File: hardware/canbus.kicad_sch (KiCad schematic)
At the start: 21 parts, among them U5 MCP2515-xSO, U6 MCP2551-I/SN, Y2 16MHz

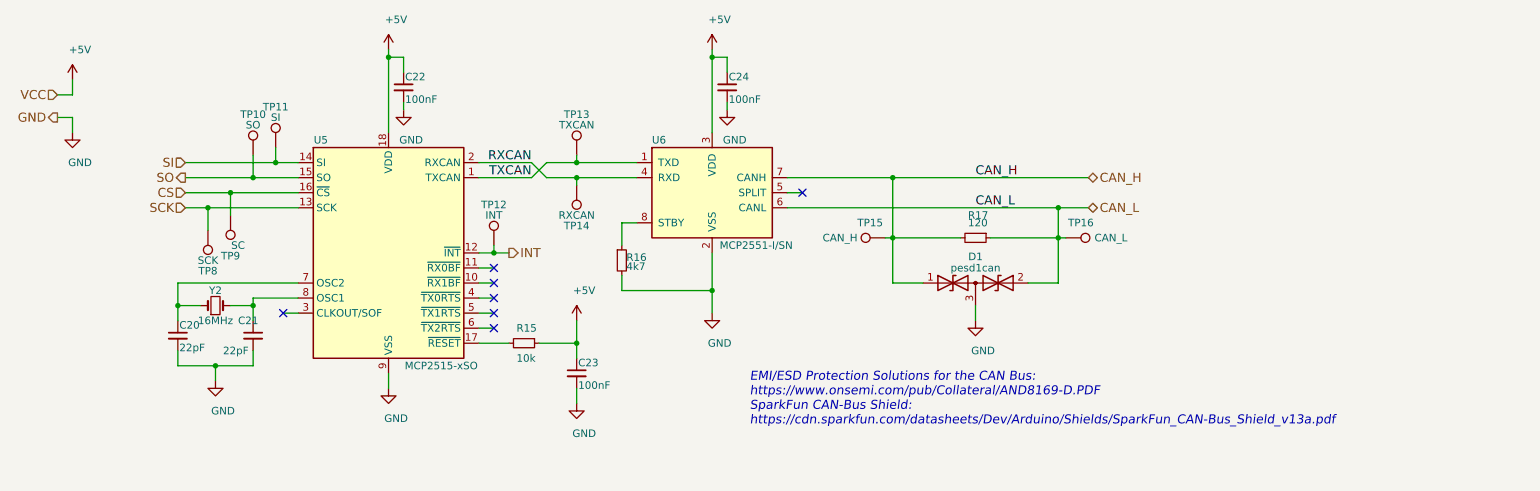
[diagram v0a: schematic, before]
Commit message: Troca do atmega328p -> STM32F103C8T Já que tem CAN integrado e ADC 12 bits (ao invés de 10)
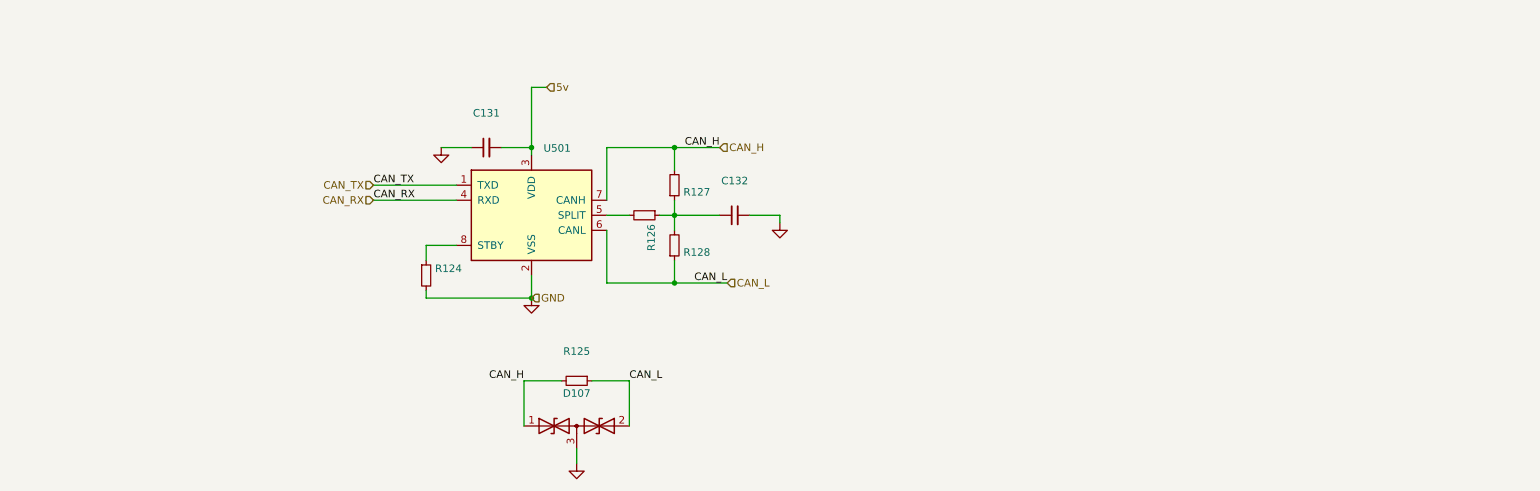
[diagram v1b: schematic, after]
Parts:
- removed C20, C21: 22pF, Capacitor_SMD:C_0805_2012Metric_Pad1.18x1.45mm_HandSolder, symbol Device:C_Small
- removed C22, C23, C24: 100nF, Capacitor_SMD:C_0805_2012Metric_Pad1.18x1.45mm_HandSolder, symbol Device:C_Small
- removed D1: pesd1can, Package_TO_SOT_SMD:SOT-23_Handsoldering, symbol Device:D_TVS_Dual_AAC
- removed R15: 10k, Resistor_SMD:R_0805_2012Metric_Pad1.20x1.40mm_HandSolder, symbol Device:R_Small
- removed R16: 4k7, Resistor_SMD:R_0805_2012Metric_Pad1.20x1.40mm_HandSolder, symbol Device:R_Small
- removed R17: 120, Resistor_SMD:R_0805_2012Metric_Pad1.20x1.40mm_HandSolder, symbol Device:R_Small
- removed TP10: SO, TestPoint:TestPoint_Pad_2.0x2.0mm, symbol Connector:TestPoint
- removed TP11: SI, TestPoint:TestPoint_Pad_2.0x2.0mm, symbol Connector:TestPoint
- removed TP12: INT, TestPoint:TestPoint_Pad_2.0x2.0mm, symbol Connector:TestPoint
- removed TP13: TXCAN, TestPoint:TestPoint_Pad_2.0x2.0mm, symbol Connector:TestPoint
- removed TP14: RXCAN, TestPoint:TestPoint_Pad_2.0x2.0mm, symbol Connector:TestPoint
- removed TP15: CAN_H, TestPoint:TestPoint_Pad_2.0x2.0mm, symbol Connector:TestPoint
- removed TP16: CAN_L, TestPoint:TestPoint_Pad_2.0x2.0mm, symbol Connector:TestPoint
- removed TP8: SCK, TestPoint:TestPoint_Pad_2.0x2.0mm, symbol Connector:TestPoint
- removed TP9: SC, TestPoint:TestPoint_Pad_2.0x2.0mm, symbol Connector:TestPoint
- removed U5: MCP2515-xSO, Package_SO:SOIC-18W_7.5x11.6mm_P1.27mm, symbol Interface_CAN_LIN:MCP2515-xSO
- removed U6: MCP2551-I/SN, Package_SO:SOIC-8_3.9x4.9mm_P1.27mm, symbol Interface_CAN_LIN:MCP2561-E-SN
- removed Y2: 16MHz, Crystal:Crystal_HC49-U_Vertical, symbol Device:Crystal_Small
- added C131, C132: (no value), symbol Device:C_Small
- added D107: ~, symbol Controle-rescue:D_TVS_x2_AAC-Device
- added R124, R125, R126, R127, R128: (no value), symbol Device:R_Small
- added U501: (no value), symbol Interface_CAN_LIN:MCP2561-E-SN
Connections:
- net CAN_H: now also D107.1 (A1), R125.2, R127.2, U501.7 (CANH)
- net CAN_L: now also D107.2 (A2), R125.1, R128.1, U501.6 (CANL)
- net GND: now also C131.1, C132.2, D107.3 (common), R124.2, U501.2 (VSS)
- new net: R124.1, U501.8 (STBY)
- new net: C132.1, R126.1, R127.1, R128.2
- new net: R126.2, U501.5 (SPLIT)
- new net 5v: C131.2, U501.3 (VDD)
- new net CAN_RX: U501.4 (RXD)
- new net CAN_TX: U501.1 (TXD)
- no-connect marks 7 -> 0
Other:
- note removed: "EMI/ESD Protection Solutions for the CAN Bus: https://www.onsemi.com/pub/Collateral/AND8169-D.PDF SparkFun CAN-Bus Shield: https://cdn.sparkfun.com/datasheets/Dev/Arduino/Shields/SparkFun_CAN-Bus_Shield_v13a.pdf"

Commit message: Primeiro protótipo da PCB
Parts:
- added TP501, TP502, TP503, TP504: (no value), symbol Connector:TestPoint
- C131: value (none) -> 100n; footprint (none) -> Capacitor_SMD:C_0603_1608Metric_Pad1.08x0.95mm_HandSolder
- C132: value (none) -> 4.7n; footprint (none) -> Capacitor_SMD:C_0603_1608Metric_Pad1.08x0.95mm_HandSolder
- D107: value ~ -> (none)
- R124: value (none) -> 4k7; footprint (none) -> Resistor_SMD:R_0603_1608Metric_Pad0.98x0.95mm_HandSolder
- R125: value (none) -> NC; footprint (none) -> Resistor_SMD:R_0603_1608Metric_Pad0.98x0.95mm_HandSolder
- R126: value (none) -> 300; footprint (none) -> Resistor_SMD:R_0603_1608Metric_Pad0.98x0.95mm_HandSolder
- R127, R128: value (none) -> 520; footprint (none) -> Resistor_SMD:R_0603_1608Metric_Pad0.98x0.95mm_HandSolder
- U501: value (none) -> MCP2561-E-SN; footprint (none) -> Package_SO:SOIC-8_3.9x4.9mm_P1.27mm
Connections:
- net CAN_H: now also TP503.1
- net CAN_L: now also TP504.1
- net CAN_RX: now also TP502.1
- net CAN_TX: now also TP501.1
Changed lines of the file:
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@@
   (junction (at 157.48 87.63) (diameter 0) (color 0 0 0 0)
   )
+  (junction (at 110.49 82.55) (diameter 0) (color 0 0 0 0)
+  )
   (junction (at 133.35 101.6) (diameter 0) (color 0 0 0 0)
   )
   (junction (at 133.35 76.2) (diameter 0) (color 0 0 0 0)
   )
+  (junction (at 110.49 85.09) (diameter 0) (color 0 0 0 0)
+  )
   (wire (pts (xy 133.35 101.6) (xy 133.35 97.79))
     (stroke (width 0) (type default) (color 0 0 0 0))
@@
     (stroke (width 0) (type default) (color 0 0 0 0))
   )
+  (wire (pts (xy 110.49 82.55) (xy 106.68 82.55))
+    (stroke (width 0) (type default) (color 0 0 0 0))
+  )
   (wire (pts (xy 140.97 129.54) (xy 140.97 127))
     (stroke (width 0) (type default) (color 0 0 0 0))
@@
     (stroke (width 0) (type default) (color 0 0 0 0))
   )
-  (wire (pts (xy 120.65 82.55) (xy 106.68 82.55))
+  (wire (pts (xy 120.65 82.55) (xy 110.49 82.55))
     (stroke (width 0) (type default) (color 0 0 0 0))
   )
@@
     (stroke (width 0) (type default) (color 0 0 0 0))
   )
+  (wire (pts (xy 110.49 85.09) (xy 106.68 85.09))
+    (stroke (width 0) (type default) (color 0 0 0 0))
+  )
   (wire (pts (xy 133.35 66.04) (xy 135.89 66.04))
     (stroke (width 0) (type default) (color 0 0 0 0))
@@
     (stroke (width 0) (type default) (color 0 0 0 0))
   )
-  (wire (pts (xy 120.65 85.09) (xy 106.68 85.09))
+  (wire (pts (xy 120.65 85.09) (xy 110.49 85.09))
     (stroke (width 0) (type default) (color 0 0 0 0))
   )
@@
       (effects (font (size 1.27 1.27)) (justify left))
     )
-    (property "Value" "" (id 1) (at 117.0686 98.933 0)
-      (effects (font (size 1.27 1.27)) (justify left))
-    )
-    (property "Footprint" "" (id 2) (at 115.57 97.79 0)
+    (property "Value" "4k7" (id 1) (at 117.0686 98.933 0)
+      (effects (font (size 1.27 1.27)) (justify left))
+    )
+    (property "Footprint" "Resistor_SMD:R_0603_1608Metric_Pad0.98x0.95mm_HandSolder" (id 2) (at 115.57 97.79 0)
       (effects (font (size 1.27 1.27)) hide)
     )
@@
     (in_bom yes) (on_board yes)
     (property "Reference" "C131" (id 0) (at 125.73 70.3834 90))
-    (property "Value" "" (id 1) (at 125.73 72.6948 90))
-    (property "Footprint" "" (id 2) (at 125.73 76.2 0)
+    (property "Value" "100n" (id 1) (at 125.73 72.6948 90))
+    (property "Footprint" "Capacitor_SMD:C_0603_1608Metric_Pad1.08x0.95mm_HandSolder" (id 2) (at 125.73 76.2 0)
       (effects (font (size 1.27 1.27)) hide)
     )
@@
     (in_bom yes) (on_board yes)
     (property "Reference" "D107" (id 0) (at 140.97 117.6782 0))
-    (property "Value" "~" (id 1) (at 140.97 119.9896 0))
+    (property "Value" "" (id 1) (at 140.97 119.9896 0))
     (property "Footprint" "" (id 2) (at 140.97 123.19 0)
       (effects (font (size 1.27 1.27)) hide)
@@
     (in_bom yes) (on_board yes)
     (property "Reference" "R125" (id 0) (at 140.97 110.5916 90))
-    (property "Value" "" (id 1) (at 140.97 112.903 90))
-    (property "Footprint" "" (id 2) (at 140.97 115.57 0)
+    (property "Value" "NC" (id 1) (at 140.97 112.903 90))
+    (property "Footprint" "Resistor_SMD:R_0603_1608Metric_Pad0.98x0.95mm_HandSolder" (id 2) (at 140.97 115.57 0)
       (effects (font (size 1.27 1.27)) hide)
     )
@@
       (effects (font (size 1.27 1.27)) (justify left))
     )
-    (property "Value" "" (id 1) (at 151.257 89.1286 0)
-      (effects (font (size 1.27 1.27)) (justify left))
-    )
-    (property "Footprint" "" (id 2) (at 152.4 87.63 0)
+    (property "Value" "300" (id 1) (at 151.257 89.1286 0)
+      (effects (font (size 1.27 1.27)) (justify left))
+    )
+    (property "Footprint" "Resistor_SMD:R_0603_1608Metric_Pad0.98x0.95mm_HandSolder" (id 2) (at 152.4 87.63 0)
       (effects (font (size 1.27 1.27)) hide)
     )
@@
       (effects (font (size 1.27 1.27)) (justify left))
     )
-    (property "Value" "" (id 1) (at 158.9786 81.407 0)
-      (effects (font (size 1.27 1.27)) (justify left))
-    )
-    (property "Footprint" "" (id 2) (at 157.48 82.55 0)
+    (property "Value" "520" (id 1) (at 158.9786 81.407 0)
+      (effects (font (size 1.27 1.27)) (justify left))
+    )
+    (property "Footprint" "Resistor_SMD:R_0603_1608Metric_Pad0.98x0.95mm_HandSolder" (id 2) (at 157.48 82.55 0)
       (effects (font (size 1.27 1.27)) hide)
     )
@@
       (effects (font (size 1.27 1.27)) (justify left))
     )
-    (property "Value" "" (id 1) (at 158.9786 91.567 0)
-      (effects (font (size 1.27 1.27)) (justify left))
-    )
-    (property "Footprint" "" (id 2) (at 157.48 92.71 0)
+    (property "Value" "520" (id 1) (at 158.9786 91.567 0)
+      (effects (font (size 1.27 1.27)) (justify left))
+    )
+    (property "Footprint" "Resistor_SMD:R_0603_1608Metric_Pad0.98x0.95mm_HandSolder" (id 2) (at 157.48 92.71 0)
       (effects (font (size 1.27 1.27)) hide)
     )
@@
     (in_bom yes) (on_board yes)
     (property "Reference" "C132" (id 0) (at 167.64 81.8134 90))
-    (property "Value" "" (id 1) (at 167.64 84.1248 90))
-    (property "Footprint" "" (id 2) (at 167.64 87.63 0)
+    (property "Value" "4.7n" (id 1) (at 167.64 84.1248 90))
+    (property "Footprint" "Capacitor_SMD:C_0603_1608Metric_Pad1.08x0.95mm_HandSolder" (id 2) (at 167.64 87.63 0)
       (effects (font (size 1.27 1.27)) hide)
     )
@@
     )
     (property "Datasheet" "" (id 3) (at 175.26 88.9 0)
+      (effects (font (size 1.27 1.27)) hide)
+    )
+    (pin "1")
+  )
+  (symbol (lib_id "Connector:TestPoint") (at 157.48 76.2 0) (unit 1)
+    (in_bom yes) (on_board yes) (fields_autoplaced)
+    (property "Reference" "TP503" (id 0) (at 158.877 72.0633 0)
+      (effects (font (size 1.27 1.27)) (justify left))
+    )
+    (property "Value" "" (id 1) (at 158.877 74.6002 0)
+      (effects (font (size 1.27 1.27)) (justify left))
+    )
+    (property "Footprint" "" (id 2) (at 162.56 76.2 0)
+      (effects (font (size 1.27 1.27)) hide)
+    )
+    (property "Datasheet" "~" (id 3) (at 162.56 76.2 0)
+      (effects (font (size 1.27 1.27)) hide)
+    )
+    (pin "1")
+  )
+  (symbol (lib_id "Connector:TestPoint") (at 157.48 99.06 180) (unit 1)
+    (in_bom yes) (on_board yes) (fields_autoplaced)
+    (property "Reference" "TP504" (id 0) (at 158.877 101.5273 0)
+      (effects (font (size 1.27 1.27)) (justify right))
+    )
+    (property "Value" "" (id 1) (at 158.877 104.0642 0)
+      (effects (font (size 1.27 1.27)) (justify right))
+    )
+    (property "Footprint" "" (id 2) (at 152.4 99.06 0)
+      (effects (font (size 1.27 1.27)) hide)
+    )
+    (property "Datasheet" "~" (id 3) (at 152.4 99.06 0)
+      (effects (font (size 1.27 1.27)) hide)
+    )
+    (pin "1")
+  )
+  (symbol (lib_id "Connector:TestPoint") (at 110.49 82.55 0) (unit 1)
+    (in_bom yes) (on_board yes) (fields_autoplaced)
+    (property "Reference" "TP501" (id 0) (at 111.887 78.4133 0)
+      (effects (font (size 1.27 1.27)) (justify left))
+    )
+    (property "Value" "" (id 1) (at 111.887 80.9502 0)
+      (effects (font (size 1.27 1.27)) (justify left))
+    )
+    (property "Footprint" "" (id 2) (at 115.57 82.55 0)
+      (effects (font (size 1.27 1.27)) hide)
+    )
+    (property "Datasheet" "~" (id 3) (at 115.57 82.55 0)
+      (effects (font (size 1.27 1.27)) hide)
+    )
+    (pin "1")
+  )
+  (symbol (lib_id "Connector:TestPoint") (at 110.49 85.09 180) (unit 1)
+    (in_bom yes) (on_board yes) (fields_autoplaced)
+    (property "Reference" "TP502" (id 0) (at 111.887 87.5573 0)
+      (effects (font (size 1.27 1.27)) (justify right))
+    )
+    (property "Value" "" (id 1) (at 111.887 90.0942 0)
+      (effects (font (size 1.27 1.27)) (justify right))
+    )
+    (property "Footprint" "" (id 2) (at 105.41 85.09 0)
+      (effects (font (size 1.27 1.27)) hide)
+    )
+    (property "Datasheet" "~" (id 3) (at 105.41 85.09 0)
       (effects (font (size 1.27 1.27)) hide)
     )
@@
       (effects (font (size 1.27 1.27)) (justify left))
     )
-    (property "Value" "" (id 1) (at 135.3694 78.8471 0)
-      (effects (font (size 1.27 1.27)) (justify left))
-    )
-    (property "Footprint" "" (id 2) (at 133.35 100.33 0)
+    (property "Value" "MCP2561-E-SN" (id 1) (at 135.3694 78.8471 0)
+      (effects (font (size 1.27 1.27)) (justify left))
+    )
+    (property "Footprint" "Package_SO:SOIC-8_3.9x4.9mm_P1.27mm" (id 2) (at 133.35 100.33 0)
       (effects (font (size 1.27 1.27) italic) hide)
     )

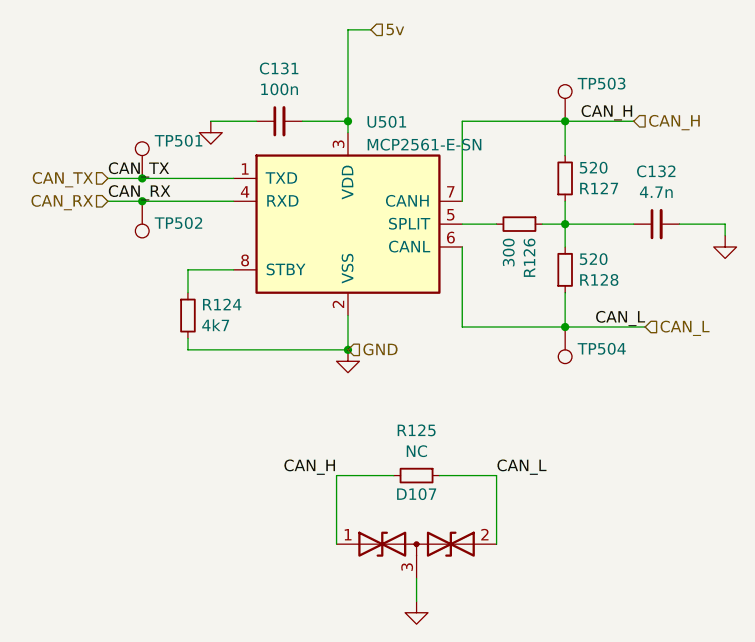
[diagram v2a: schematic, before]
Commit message: hardware: STM32, PCB design in progress
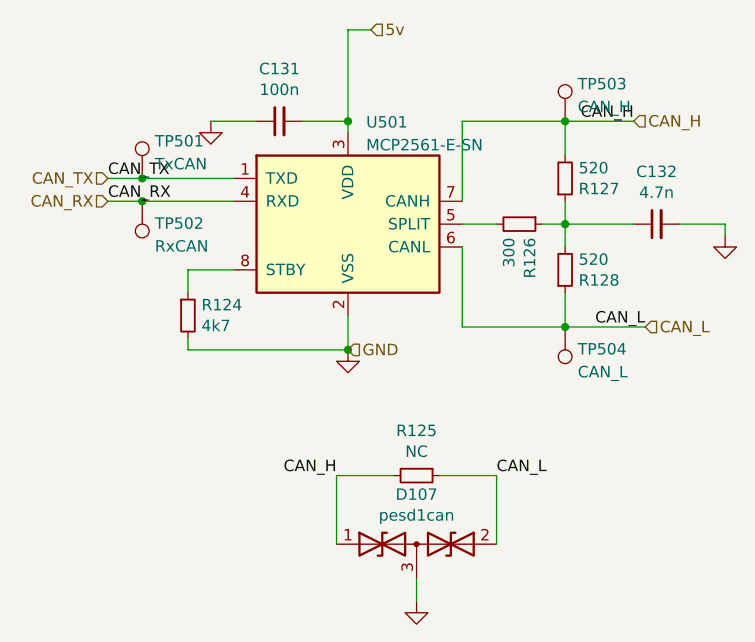
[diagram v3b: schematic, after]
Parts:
- D107: value (none) -> pesd1can; footprint (none) -> Package_TO_SOT_SMD:SOT-23
- TP501: value (none) -> TxCAN; footprint (none) -> TestPoint:TestPoint_Pad_2.0x2.0mm
- TP502: value (none) -> RxCAN; footprint (none) -> TestPoint:TestPoint_Pad_2.0x2.0mm
- TP503: value (none) -> CAN_H; footprint (none) -> TestPoint:TestPoint_Pad_2.0x2.0mm
- TP504: value (none) -> CAN_L; footprint (none) -> TestPoint:TestPoint_Pad_2.0x2.0mm
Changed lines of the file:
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@@
     (in_bom yes) (on_board yes)
     (property "Reference" "D107" (id 0) (at 140.97 117.6782 0))
-    (property "Value" "" (id 1) (at 140.97 119.9896 0))
-    (property "Footprint" "" (id 2) (at 140.97 123.19 0)
+    (property "Value" "pesd1can" (id 1) (at 140.97 119.9896 0))
+    (property "Footprint" "Package_TO_SOT_SMD:SOT-23" (id 2) (at 140.97 123.19 0)
       (effects (font (size 1.27 1.27)) hide)
     )
@@
       (effects (font (size 1.27 1.27)) (justify left))
     )
-    (property "Value" "" (id 1) (at 158.877 74.6002 0)
+    (property "Value" "CAN_H" (id 1) (at 158.877 74.6002 0)
       (effects (font (size 1.27 1.27)) (justify left))
     )
-    (property "Footprint" "" (id 2) (at 162.56 76.2 0)
+    (property "Footprint" "TestPoint:TestPoint_Pad_2.0x2.0mm" (id 2) (at 162.56 76.2 0)
       (effects (font (size 1.27 1.27)) hide)
     )
@@
       (effects (font (size 1.27 1.27)) (justify right))
     )
-    (property "Value" "" (id 1) (at 158.877 104.0642 0)
+    (property "Value" "CAN_L" (id 1) (at 158.877 104.0642 0)
       (effects (font (size 1.27 1.27)) (justify right))
     )
-    (property "Footprint" "" (id 2) (at 152.4 99.06 0)
+    (property "Footprint" "TestPoint:TestPoint_Pad_2.0x2.0mm" (id 2) (at 152.4 99.06 0)
       (effects (font (size 1.27 1.27)) hide)
     )
@@
       (effects (font (size 1.27 1.27)) (justify left))
     )
-    (property "Value" "" (id 1) (at 111.887 80.9502 0)
+    (property "Value" "TxCAN" (id 1) (at 111.887 80.9502 0)
       (effects (font (size 1.27 1.27)) (justify left))
     )
-    (property "Footprint" "" (id 2) (at 115.57 82.55 0)
+    (property "Footprint" "TestPoint:TestPoint_Pad_2.0x2.0mm" (id 2) (at 115.57 82.55 0)
       (effects (font (size 1.27 1.27)) hide)
     )
@@
       (effects (font (size 1.27 1.27)) (justify right))
     )
-    (property "Value" "" (id 1) (at 111.887 90.0942 0)
+    (property "Value" "RxCAN" (id 1) (at 111.887 90.0942 0)
       (effects (font (size 1.27 1.27)) (justify right))
     )
-    (property "Footprint" "" (id 2) (at 105.41 85.09 0)
+    (property "Footprint" "TestPoint:TestPoint_Pad_2.0x2.0mm" (id 2) (at 105.41 85.09 0)
       (effects (font (size 1.27 1.27)) hide)
     )
